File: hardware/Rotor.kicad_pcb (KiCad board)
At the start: 2 copper layers, 200 x 200 mm, 0 parts

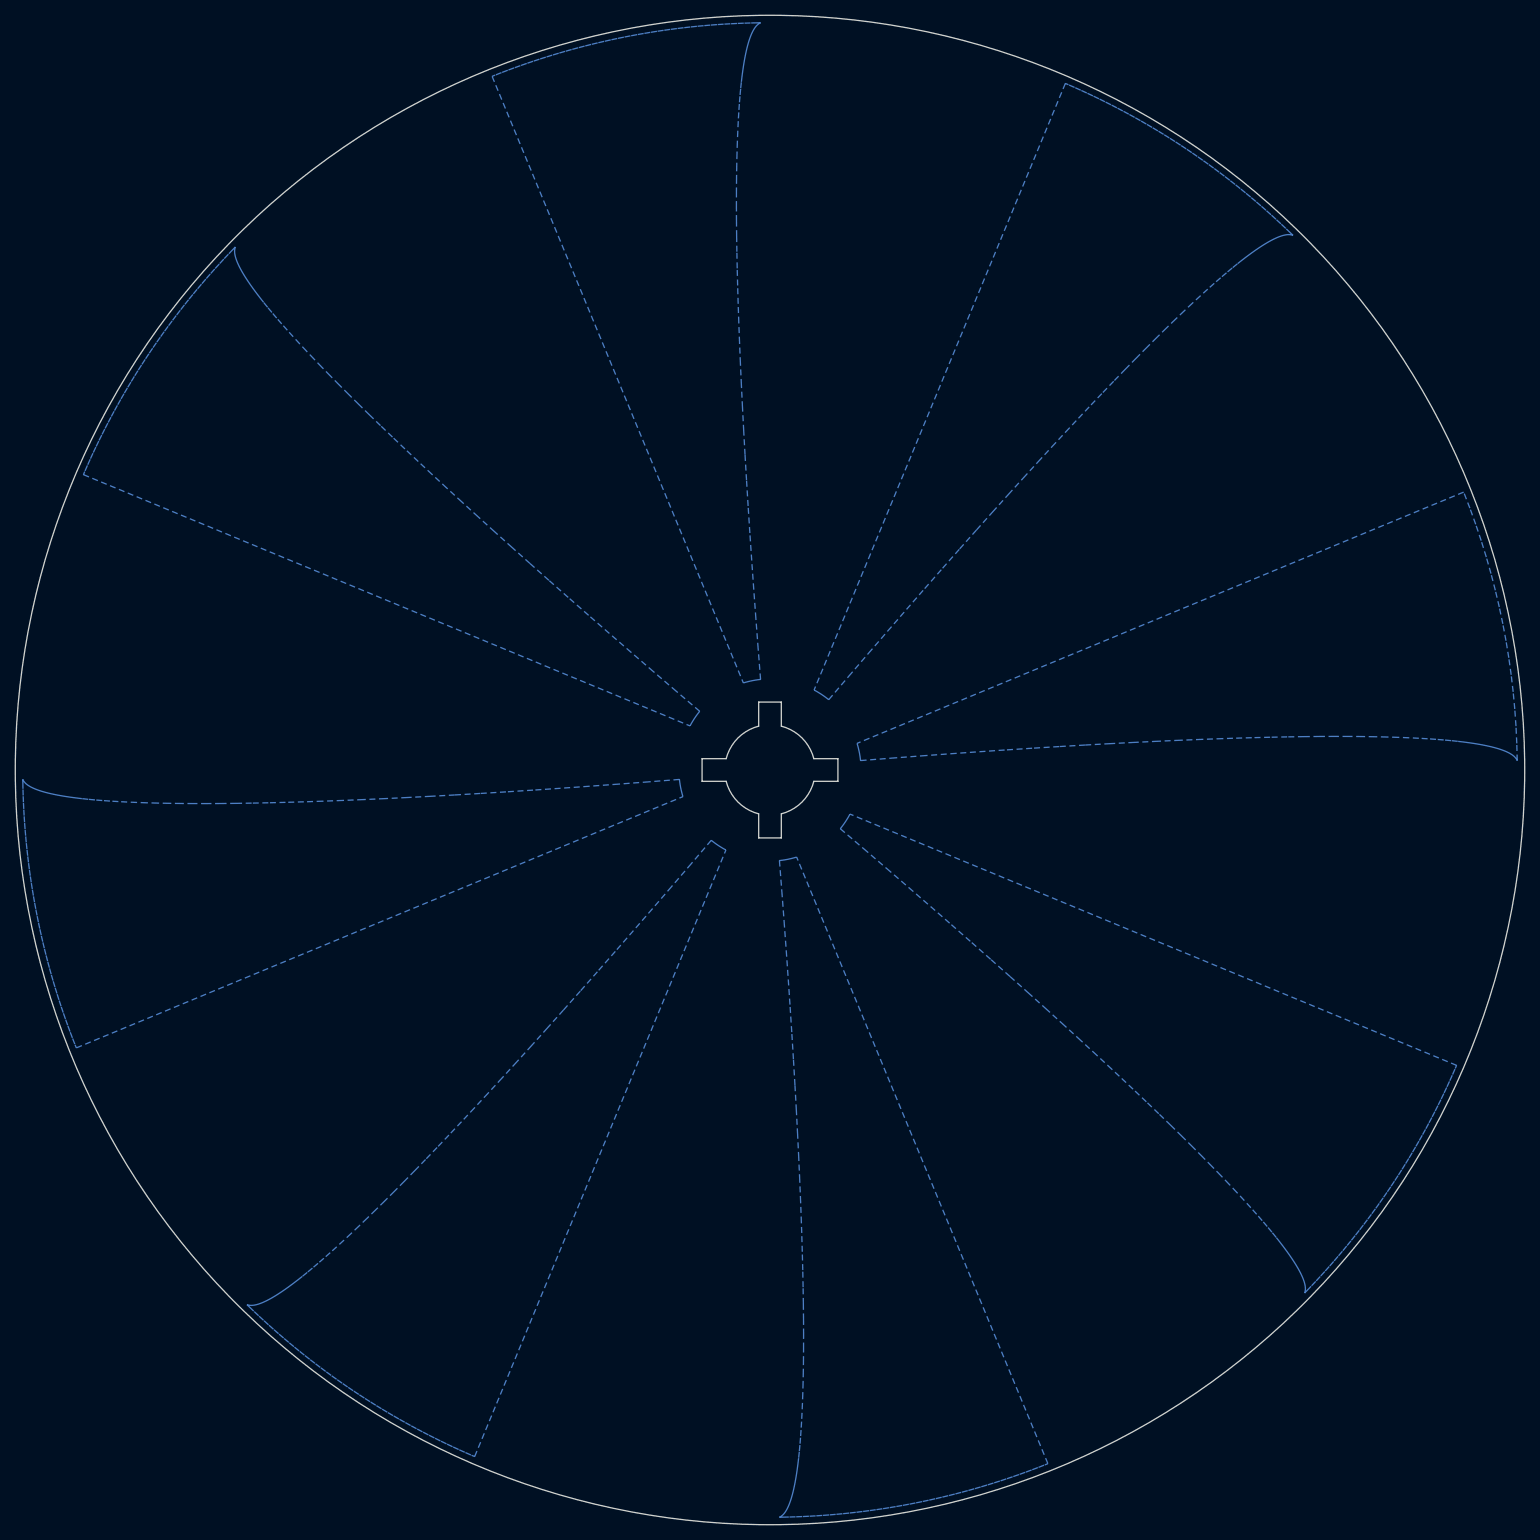
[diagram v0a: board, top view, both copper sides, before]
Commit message: Generator design
Updated the rotor design.
Updated the stator design.
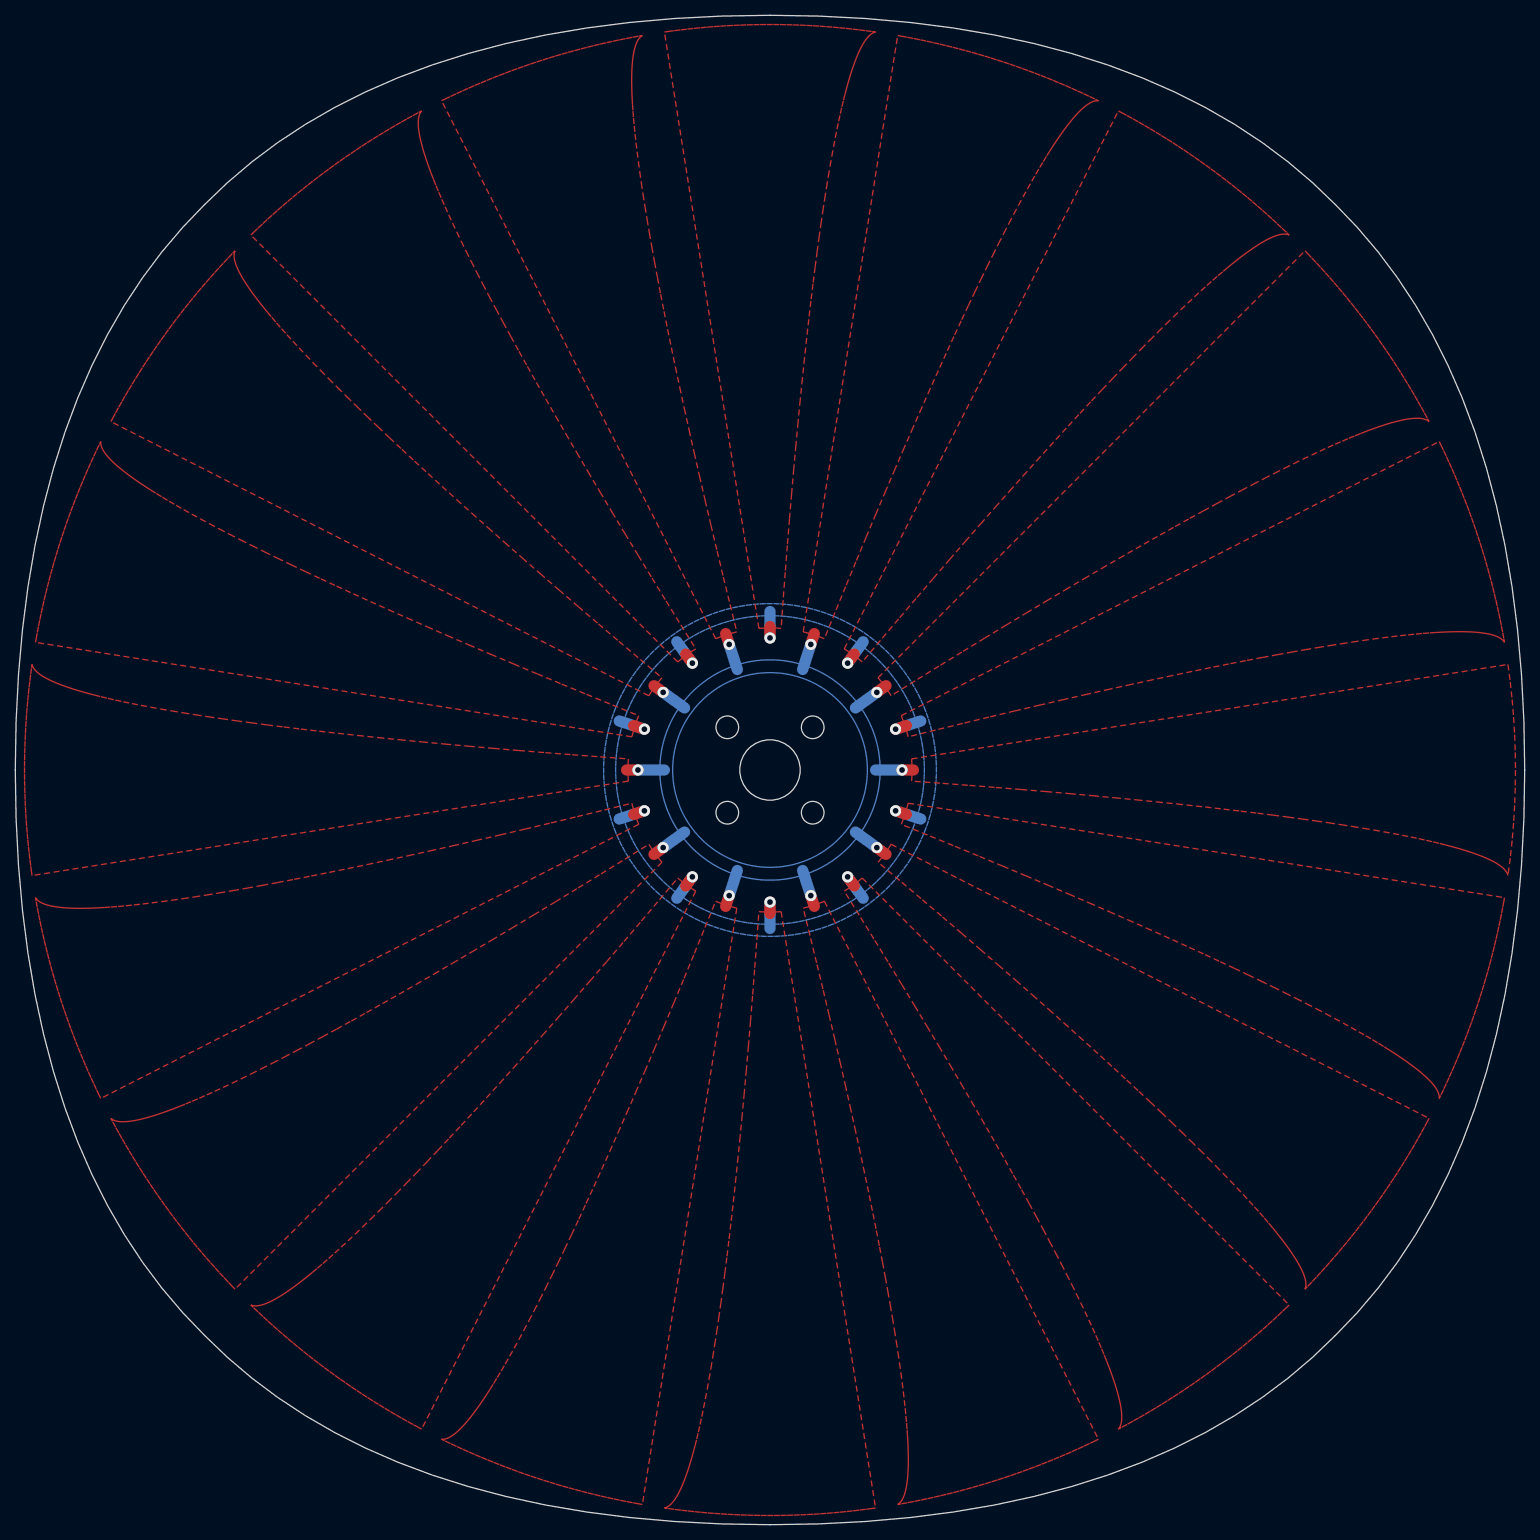
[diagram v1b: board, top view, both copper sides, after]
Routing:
- net B: track 0.00 -> 50.0 mm, vias 0 -> 10
- net A: track 0.00 -> 50.0 mm, vias 0 -> 10
- added copper zone on B.Cu, net A
- added copper zone on F.Cu, net A
- added copper zone on B.Cu, net B
- added copper zone on F.Cu, net B
- removed copper zone on B.Cu, net (none)
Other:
- outline, holes or cut-outs redrawn
